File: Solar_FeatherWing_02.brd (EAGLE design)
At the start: 50.8 x 22.9 mm, 39 parts, among them IC1 SPV1040T, IC2 TPL5111, J1 1X2-3.5MM, SW2 SW-K3-1290S-J1

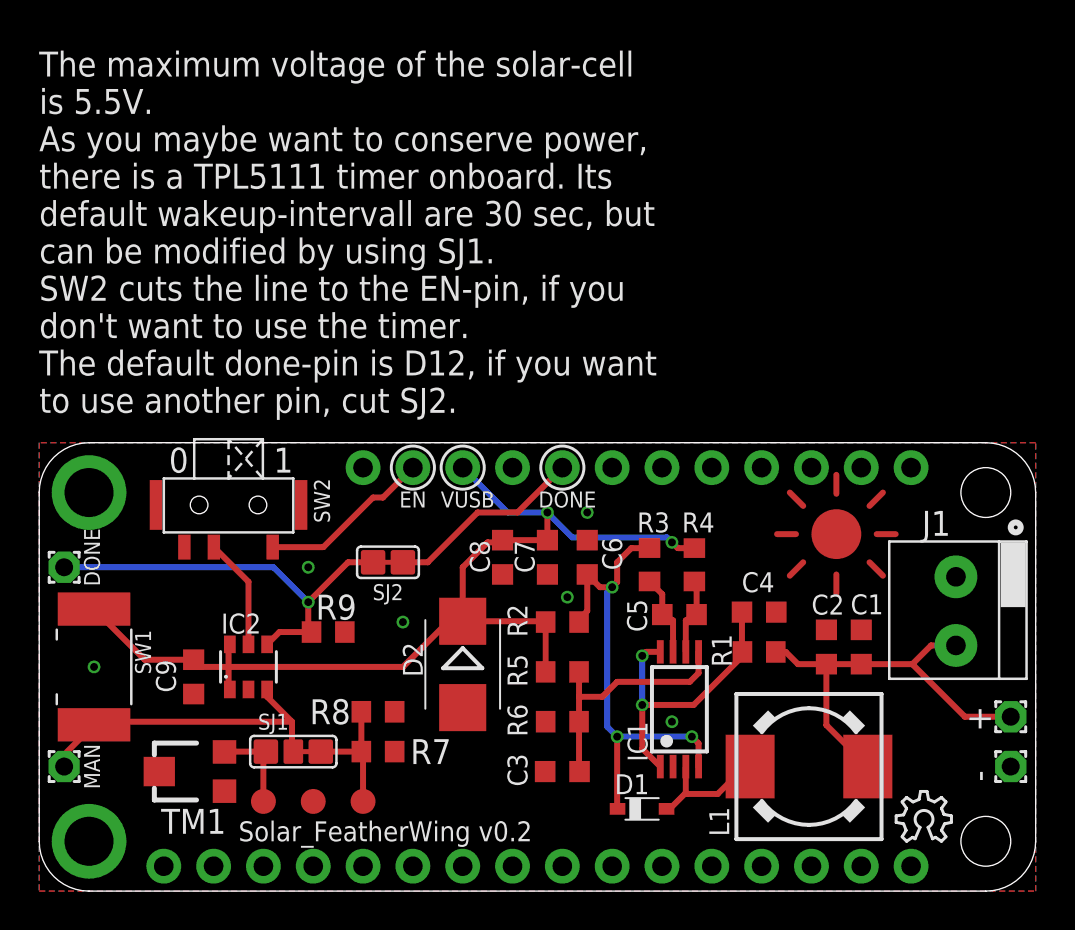
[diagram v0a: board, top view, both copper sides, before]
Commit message: Changed features
Removed the timer-ic and added a INA219 to monitor power.
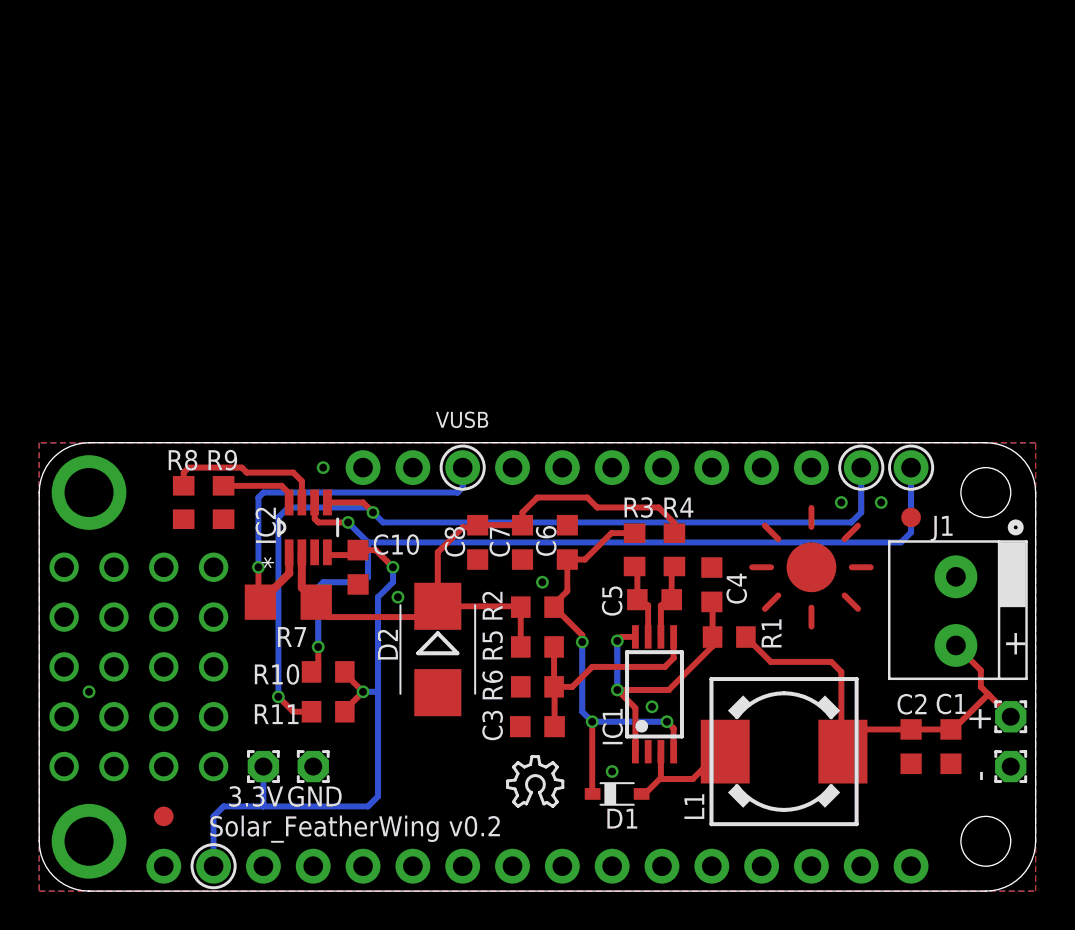
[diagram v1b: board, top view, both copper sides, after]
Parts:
- removed C9: 1uF, rcl:C0603K
- removed DONE: DONE, wirepad:1,6/0,9
- removed MAN: MAN, wirepad:1,6/0,9
- removed SJ1: JUMPER3-0603-NC, we-rcl:JUMPER3-0603_NC
- removed SJ2: JUMPER2-0603-NC, we-rcl:JUMPER2-0603_NC
- removed SW1: (no value), adafruit:BTN_CK_KSS
- removed SW2: SW-K3-1290S-J1, _RTC-Lib:SW-K3-1290S-J1
- removed TM1: (no value), adafruit:TC33X
- removed TP1, TP2, TP3: TPB1,27, testpad:B1,27
- added 3.3V, GND: (no value), wirepad:1,6/0,9
- added C10: 100nF, rcl:C0603K
- added R10, R11: 4.7k, rcl:R0603
- added U$2, U$3: FIDUCIAL, adafruit:FIDUCIAL_1MM
- D1: value BAT60J -> NSR0530HT1G
- D2: value (none) -> SMBJ5339B-TP
- IC2: value TPL5111 -> INA219AIDCNR; device _RTC-Lib:SOT23-6 -> Texas Instruments_By_element14_Batch_1:SOT65P280X145-8N
- R2: value 820m -> 50m
- R7: value 32.4k -> (none); device rcl:R0603 -> rcl:R1206
- R8: value 34.8k -> 10k
- R9: value 1.2M -> 10k
- moved LOGO1 19.9 mm to (23.9, 4.32)
- moved R8 14.6 mm to (7.37, 19.8), turned to 270 degrees
- moved R7 8.89 mm to (12.7, 14.7)
- moved R9 8.49 mm to (9.40, 19.8), turned to 270 degrees
- moved IC2 7.74 mm to (13.7, 18.5), turned to 90 degrees
- moved C1 6.83 mm to (46.5, 7.37), turned to 270 degrees
- moved C2 6.67 mm to (44.5, 7.37), turned to 270 degrees
- moved C4 2.79 mm to (34.3, 15.6), turned to 90 degrees
- moved C3 2.62 mm to (25.4, 8.38)
- moved R6 2.18 mm to (25.4, 10.4)
- moved U$1 2.11 mm to (39.4, 16.5)
- moved R5 1.80 mm to (25.4, 12.4)
- moved R1 1.70 mm to (35.2, 13.0)
- moved C5 1.48 mm to (31.4, 14.9)
- moved D1 1.48 mm to (29.5, 4.95)
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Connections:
- removed net N$6: IC2.5, SW2.P2I
- removed net N$8: SJ1.3, TM1.3, TP1.TP
- removed net N$9: IC2.3, MAN.1, R7.1, R8.1, SJ1.1, SJ1.2, SW1.P$2, TP2.TP
- new net 3V: 3.3V.1, C10.1, IC2.4, MS1.2, R10.1, R11.1
- new net N$35: IC2.8, R9.1
- new net N$36: IC2.7, R8.1
- new net SCL: IC2.5, MS1.18, R11.2
- new net SDA: IC2.6, MS1.17, R10.2
- new net USB: IC2.1, MS1.26, R7.1
- net +5V: now also IC2.2, R7.2; no longer C9.1, IC2.1, IC2.6, MS1.26, SW1.P$1
- net DONE_DEF: no longer DONE.1, IC2.4, R9.1, SJ2.1, SJ2.2
- net EN_PIN: no longer SW2.P3O
- net GND: now also C10.2, GND.1, IC2.3; no longer C9.2, IC2.2, R7.2, TM1.2, TP3.TP
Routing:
- net SCL: track 0.00 -> 46.4 mm, vias 0 -> 2
- net SDA: track 0.00 -> 44.2 mm, vias 0 -> 2
- net DONE_DEF: track 33.1 -> 0.00 mm, vias 1 -> 0
- net 3V: track 0.00 -> 32.8 mm, vias 0 -> 2
- net N$9: track 24.7 -> 0.00 mm, vias 0 -> 1
- net USB: track 0.00 -> 20.2 mm, vias 0 -> 1
- net +5V: track 54.3 -> 35.1 mm, vias 2 -> 0
- net EN_PIN: track 8.83 -> 0.00 mm
- net N$36: track 0.00 -> 8.18 mm
- net N$6: track 5.69 -> 0.00 mm, vias 0 -> 1
- net N$8: track 4.71 -> 0.00 mm, vias 0 -> 1
- net N$35: track 0.00 -> 3.97 mm
- net N$7: track 24.6 -> 22.7 mm
- net N_PV+: track 22.1 -> 24.0 mm
- net N_VCTRL: track 13.0 -> 11.9 mm
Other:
- board text added: "+"
- board text added: "Sources and description: https://github.com/glx-seven/Solar_FeatherWing"
- board text removed: "0"
- board text removed: "1"
- board text removed: "DONE"
- board text removed: "EN"
- board text removed: "The maximum voltage of the solar-cell is 5.5V. As you maybe want to conserve power, there is a TPL5111 timer onboard. Its default wakeup-intervall are 30 sec, but can be modified by using SJ1. SW2 cuts the line to the EN-pin, if you don't want to use the timer. The default done-pin is D12, if you want to use another pin, cut SJ2."

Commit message: Monitor battery current and voltage
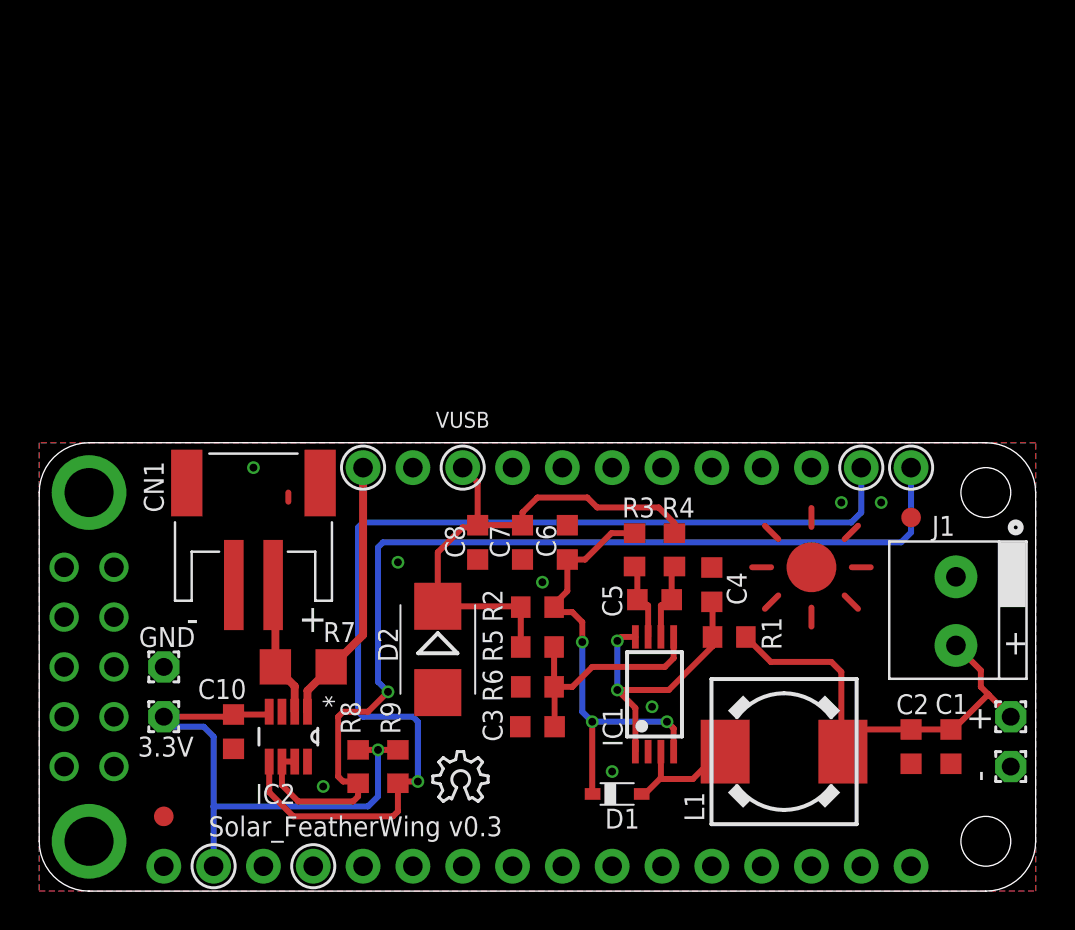
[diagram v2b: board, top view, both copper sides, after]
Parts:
- removed R10, R11: 4.7k, rcl:R0603
- added CN1: (no value), adafruit:JST-PH-2-SMT-RA
- R8, R9: value 10k -> 4.7k
- moved R8 16.1 mm to (16.3, 6.35)
- moved R9 16.1 mm to (18.3, 6.35)
- moved IC2 10.7 mm to (12.7, 7.87), turned to 270 degrees
- moved C10 10.5 mm to (9.91, 8.13)
- moved GND 9.16 mm to (6.35, 11.4)
- moved 3.3V 5.68 mm to (6.35, 8.89)
- moved LOGO1 3.82 mm to (20.1, 4.57)
- moved R7 3.39 mm to (13.5, 11.4), turned to 180 degrees
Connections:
- removed net N$35: IC2.8, R9.1
- removed net N$36: IC2.7, R8.1
- removed net USB: IC2.1, MS1.26, R7.1
- new net N$15: CN1.1, IC2.2, R7.2
- new net VBAT: IC2.1, MS1.28, R7.1
- net +5V: now also MS1.26; no longer IC2.2, R7.2
- net 3V: now also R8.1, R9.1; no longer R10.1, R11.1
- net GND: now also CN1.2, IC2.8; no longer R8.2, R9.2
- net SCL: now also R9.2; no longer R11.2
- net SDA: now also IC2.7, R8.2; no longer R10.2
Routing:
- net USB: track 20.2 -> 0.00 mm, vias 1 -> 0
- net VBAT: track 0.00 -> 13.6 mm
- net SCL: track 46.4 -> 55.2 mm, vias 2 -> 1
- net SDA: track 44.2 -> 52.5 mm, vias 2 -> 1
- net N$36: track 8.18 -> 0.00 mm
- net N$15: track 0.00 -> 6.92 mm, vias 1 -> 0
- net +5V: track 35.1 -> 28.5 mm
- net 3V: track 32.8 -> 28.2 mm, vias 2 -> 1
- net N$35: track 3.97 -> 0.00 mm
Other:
- board text added: "Solar_FeatherWing v0.3"
- board text removed: "Solar_FeatherWing v0.2"
